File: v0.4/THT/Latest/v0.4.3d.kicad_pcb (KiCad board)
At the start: 2 copper layers, 92 x 100 mm, 116 parts, among them IC3 Trig Cond Socket, J1 Conn_01x05, J10 Conn_01x03, J3 Conn_01x02, J5 Conn_01x04, J6 Conn_01x05, J8 Conn_01x03, Q1 LFPAK88, Q3 LFPAK88, U1 SP721, U2 TC4424A, U3 SP721, U6 ULN2003, U8 LM2940S-5.0

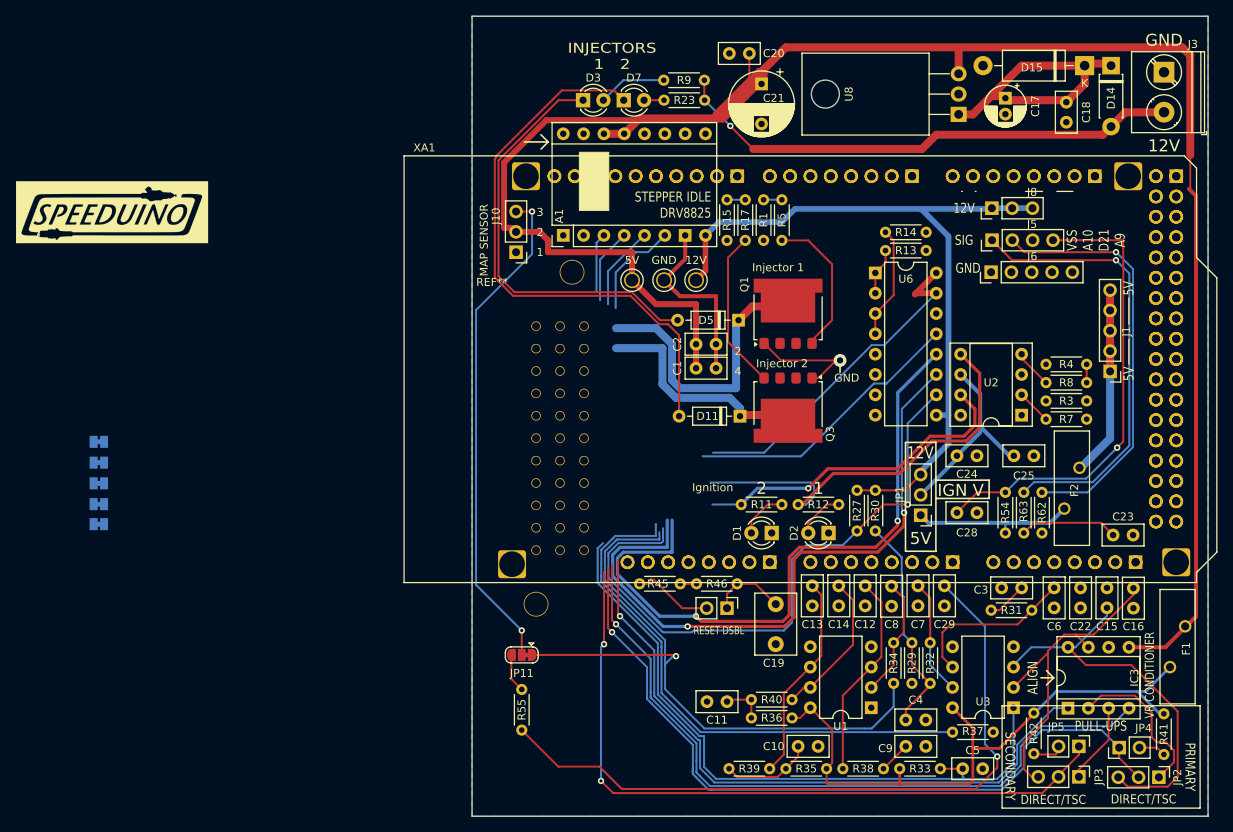
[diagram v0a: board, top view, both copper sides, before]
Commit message: split to 4v-mini
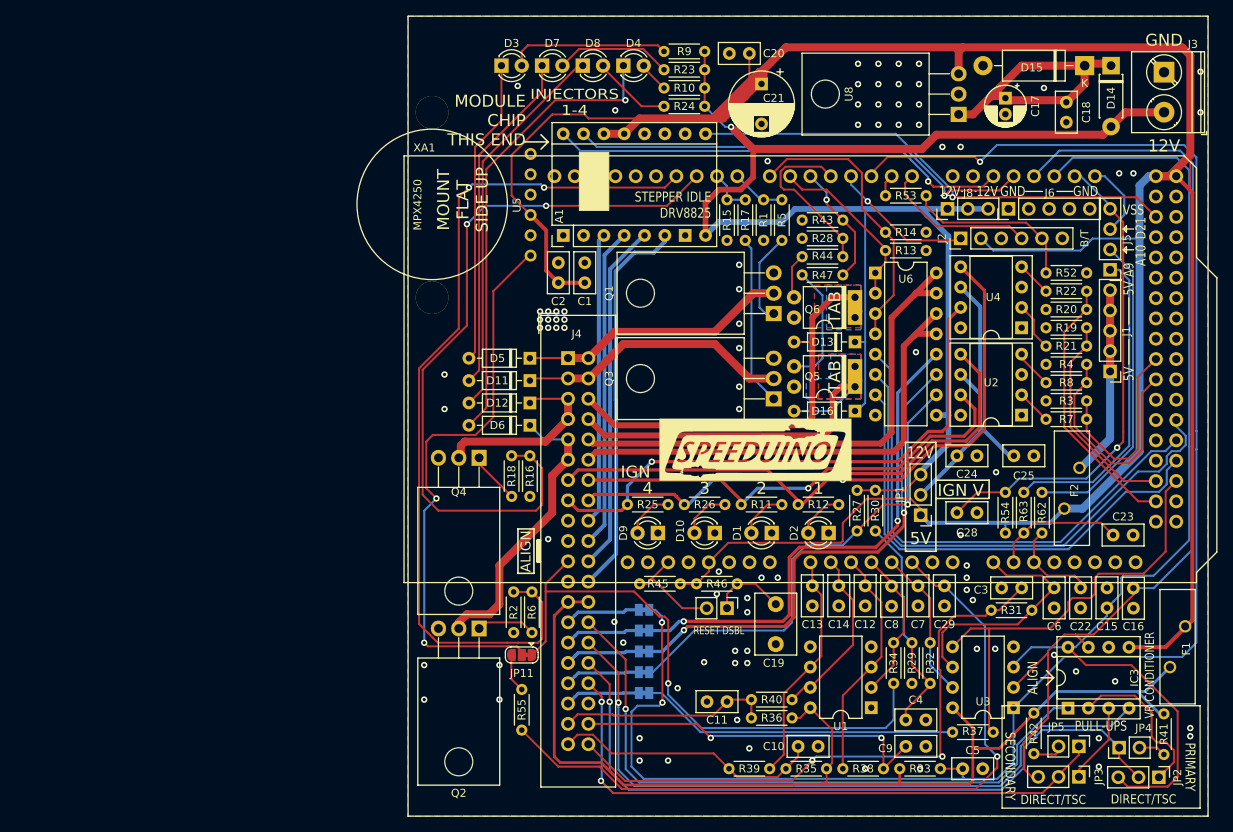
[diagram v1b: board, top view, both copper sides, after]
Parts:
- removed 12V, 5V, GND: TestPoint_Keystone_5000-5004_Miniature, TestPoint:TestPoint_Keystone_5000-5004_Miniature
- removed ? (x4): , 
- removed J10: Conn_01x03, Connector_PinHeader_2.54mm:PinHeader_1x03_P2.54mm_Vertical
- removed REF**: 6189-7106, user-made:6189-7106
- removed REF** (x5): PinHeader_1x08_P2.54mm_Vertical, Connector_PinHeader_2.54mm:PinHeader_1x08_P2.54mm_Vertical
- removed REF**: PinHeader_1x10_P2.54mm_Vertical, Connector_PinHeader_2.54mm:PinHeader_1x10_P2.54mm_Vertical
- removed REF**: PinHeader_2x18_P2.54mm_Vertical, Connector_PinHeader_2.54mm:PinHeader_2x18_P2.54mm_Vertical
- added D10: LED, LED_THT:LED_D3.0mm, F.Cu at (148.8, 101.6)
- added D12: D, Diode_THT:D_DO-35_SOD27_P7.62mm_Horizontal, F.Cu at (125.7, 85.3)
- added D13: D, Diode_THT:D_DO-35_SOD27_P7.62mm_Horizontal, F.Cu at (166.4, 77.7)
- added D16: D, Diode_THT:D_DO-35_SOD27_P7.62mm_Horizontal, F.Cu at (166.4, 86.4)
- added D4: LED, LED_THT:LED_D3.0mm, F.Cu at (137.4, 43.2)
- added D6: D, Diode_THT:D_DO-35_SOD27_P7.62mm_Horizontal, F.Cu at (125.7, 88.1)
- added D8: LED, LED_THT:LED_D3.0mm, F.Cu at (132.3, 43.2)
- added D9: LED, LED_THT:LED_D3.0mm, F.Cu at (141.7, 101.6)
- added J2: Conn_01x06, Connector_PinHeader_2.54mm:PinHeader_1x06_P2.54mm_Vertical, F.Cu at (179.6, 64.8)
- added J4: Conn_02x20_Counter_Clockwise, Connector_IDC:IDC-Header_2x20_P2.54mm_Vertical, F.Cu at (130.5, 79.7)
- added Q2: Q_NMOS_GDS, Package_TO_SOT_THT:TO-220-3_Horizontal_TabDown, F.Cu at (119.4, 113.5)
- added Q4: Q_NMOS_GDS, Package_TO_SOT_THT:TO-220-3_Horizontal_TabDown, F.Cu at (119.4, 92.2)
- added Q5: Q_NMOS_GDSD, Package_DIP:Vishay_HVM-DIP-3_W7.62mm, F.Cu at (166.4, 83.3)
- added Q6: Q_NMOS_GDSD, Package_DIP:Vishay_HVM-DIP-3_W7.62mm, F.Cu at (166.4, 74.7)
- added R10: 2.4k, Resistor_THT:R_Axial_DIN0204_L3.6mm_D1.6mm_P5.08mm_Horizontal, F.Cu at (142.5, 46.0)
- added R16: 100k, Resistor_THT:R_Axial_DIN0204_L3.6mm_D1.6mm_P5.08mm_Horizontal, F.Cu at (125.7, 97.0)
- added R18: 1k, Resistor_THT:R_Axial_DIN0204_L3.6mm_D1.6mm_P5.08mm_Horizontal, F.Cu at (123.4, 97.0)
- added R19: 100k, Resistor_THT:R_Axial_DIN0204_L3.6mm_D1.6mm_P5.08mm_Horizontal, F.Cu at (195.3, 75.9)
- added R2: 100k, Resistor_THT:R_Axial_DIN0204_L3.6mm_D1.6mm_P5.08mm_Horizontal, F.Cu at (123.7, 114.0)
- added R20: 100k, Resistor_THT:R_Axial_DIN0204_L3.6mm_D1.6mm_P5.08mm_Horizontal, F.Cu at (190.2, 73.7)
- added R21: 1k, Resistor_THT:R_Axial_DIN0204_L3.6mm_D1.6mm_P5.08mm_Horizontal, F.Cu at (190.2, 78.2)
- added R22: 1k, Resistor_THT:R_Axial_DIN0204_L3.6mm_D1.6mm_P5.08mm_Horizontal, F.Cu at (190.2, 71.4)
- added R24: 2.4k, Resistor_THT:R_Axial_DIN0204_L3.6mm_D1.6mm_P5.08mm_Horizontal, F.Cu at (142.5, 48.3)
- added R25: 2.4k, Resistor_THT:R_Axial_DIN0204_L3.6mm_D1.6mm_P5.08mm_Horizontal, F.Cu at (137.9, 98.0)
- added R26: 2.4k, Resistor_THT:R_Axial_DIN0204_L3.6mm_D1.6mm_P5.08mm_Horizontal, F.Cu at (145.0, 98.0)
- added R28: 100k, Resistor_THT:R_Axial_DIN0204_L3.6mm_D1.6mm_P5.08mm_Horizontal, F.Cu at (159.8, 64.8)
- added R43: 100k, Resistor_THT:R_Axial_DIN0204_L3.6mm_D1.6mm_P5.08mm_Horizontal, F.Cu at (159.8, 62.5)
- added R44: 1k, Resistor_THT:R_Axial_DIN0204_L3.6mm_D1.6mm_P5.08mm_Horizontal, F.Cu at (164.8, 67.1)
- added R47: 1k, Resistor_THT:R_Axial_DIN0204_L3.6mm_D1.6mm_P5.08mm_Horizontal, F.Cu at (164.8, 69.3)
- added R52: 2k, Resistor_THT:R_Axial_DIN0204_L3.6mm_D1.6mm_P5.08mm_Horizontal, F.Cu at (190.2, 69.1)
- added R53: 1k, Resistor_THT:R_Axial_DIN0204_L3.6mm_D1.6mm_P5.08mm_Horizontal, F.Cu at (170.2, 59.4)
- added R6: 1k, Resistor_THT:R_Axial_DIN0204_L3.6mm_D1.6mm_P5.08mm_Horizontal, F.Cu at (126.0, 114.0)
- added U4: TC4424A, Package_DIP:DIP-8_W7.62mm_Socket, F.Cu at (187.2, 75.9)
- added U5: MPX4250, Misc:MPX4250, F.Cu at (125.8, 66.9)
- Q1, Q3: value LFPAK88 -> Q_NMOS_GDS; footprint Package_TO_SOT_SMD:LFPAK88 -> Package_TO_SOT_THT:TO-220-3_Horizontal_TabDown
- moved G*** 85.7 mm to (153.9, 91.2)
- moved JP10 72.1 mm to (140.0, 121.6)
- moved JP7 72.1 mm to (140.0, 113.8)
- moved JP8 72.1 mm to (140.0, 116.4)
- moved JP9 72.1 mm to (140.0, 119.0)
- moved JP6 69.0 mm to (140.0, 111.2)
- moved D11 26.6 mm to (125.7, 82.5)
- moved D5 26.5 mm to (125.7, 79.8)
- moved C2 22.2 mm to (129.3, 67.8), turned to 270 degrees
- moved C1 21.1 mm to (132.6, 67.8), turned to 270 degrees
- moved J5 15.2 mm to (198.3, 68.7), turned to 180 degrees
- moved D7 11.1 mm to (127.3, 43.2)
- moved D3 11.1 mm to (122.2, 43.2)
- moved J6 8.21 mm to (185.6, 61.1)
- moved J8 5.54 mm to (177.9, 61.1)
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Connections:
- Q1 pad 1: GND -> Net-(Q1-Pad1)
- Q1 pad 2: (no net) -> INJ-1-OUT
- Q1 pad 3: (no net) -> GND
- Q3 pad 1: GND -> Net-(Q3-Pad1)
- Q3 pad 2: (no net) -> INJ-2-OUT
- Q3 pad 3: (no net) -> GND
- XA1 pad D0: (no net) -> MCU-D0
- XA1 pad D1: (no net) -> MCU-D1
- XA1 pad D3: (no net) -> MCU-D3
- XA1 pad D4: (no net) -> MCU-D4
- XA1 pad D5: (no net) -> MCU-D5
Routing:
- net ADC-Clamp-7: track 85.3 -> 215.0 mm, vias 0 -> 3
- net MCU-D11: track 0.00 -> 109.2 mm, vias 0 -> 2
- net MCU-D10: track 0.00 -> 92.4 mm, vias 0 -> 2
- net VDD: track 266.0 -> 355.9 mm
- net ADC-Clamp-9: track 49.1 -> 128.8 mm
- net ADC-Clamp-8: track 40.9 -> 120.5 mm
- net IGN-3-OUT: track 0.00 -> 75.8 mm, vias 0 -> 1
- net O2_Sensor: track 4.97 -> 75.9 mm, vias 0 -> 2
- net IGN-4-OUT: track 0.00 -> 69.2 mm, vias 0 -> 1
- net MCU-D45: track 0.00 -> 67.7 mm
- net MCU-D47: track 0.00 -> 64.4 mm
- net MCU-D24: track 0.00 -> 61.1 mm, vias 0 -> 1
- net MCU-D49: track 0.00 -> 60.7 mm
- net VDDA: track 77.6 -> 136.4 mm
- net MCU-D17: track 0.00 -> 58.6 mm, vias 0 -> 1
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- added copper zone on F.Cu, net GND
- added copper zone on B.Cu, net HC-2-OUT
- added copper zone on F.Cu, net HC-2-OUT
- added copper zone on B.Cu, net IDLE-OUT
- added copper zone on F.Cu, net IDLE-OUT
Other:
- board size 92 x 100 mm -> 100 x 100 mm
- net class Default added: clearance 0.2, trace_width 0.25, via_dia 0.8, via_drill 0.4
- board text added: "B/T"
- board text added: "IGN"
- board text added: "INJECTORS 1-4"
- board text added: "MODULE CHIP THIS END"
- board text added: "MOUNT FLAT SIDE UP"
- board text added: "TAB"
- board text removed: "1"
- board text removed: "2"
- board text removed: "3"
- board text removed: "4"
- board text removed: "INJECTORS 1 2"
- board text removed: "Ignition"
- board text removed: "Injector 1"
- board text removed: "Injector 2"
- board text removed: "MAP SENSOR"
- board text removed: "REV 0.0.1 - diarmuid kelly 2025"
- board text removed: "SIG"

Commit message: kicad work
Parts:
- removed D10, D4, D8, D9: LED, LED_THT:LED_D3.0mm
- removed D12, D13, D16, D6: D, Diode_THT:D_DO-35_SOD27_P7.62mm_Horizontal
- removed J2: Conn_01x06, Connector_PinHeader_2.54mm:PinHeader_1x06_P2.54mm_Vertical
- removed J4: Conn_02x20_Counter_Clockwise, Connector_IDC:IDC-Header_2x20_P2.54mm_Vertical
- removed Q2, Q4: Q_NMOS_GDS, Package_TO_SOT_THT:TO-220-3_Horizontal_TabDown
- removed Q5, Q6: Q_NMOS_GDSD, Package_DIP:Vishay_HVM-DIP-3_W7.62mm
- removed R10, R24, R25, R26: 2.4k, Resistor_THT:R_Axial_DIN0204_L3.6mm_D1.6mm_P5.08mm_Horizontal
- removed R16, R19, R2, R20, R28, R43: 100k, Resistor_THT:R_Axial_DIN0204_L3.6mm_D1.6mm_P5.08mm_Horizontal
- removed R18, R21, R22, R44, R47, R53, R6: 1k, Resistor_THT:R_Axial_DIN0204_L3.6mm_D1.6mm_P5.08mm_Horizontal
- removed R52: 2k, Resistor_THT:R_Axial_DIN0204_L3.6mm_D1.6mm_P5.08mm_Horizontal
- removed U4: TC4424A, Package_DIP:DIP-8_W7.62mm_Socket
- removed U5: MPX4250, Misc:MPX4250
- added 12V: TestPoint_Keystone_5000-5004_Miniature, TestPoint:TestPoint_Keystone_5000-5004_Miniature, F.Cu at (146.5, 70.0)
- added 5V: TestPoint_Keystone_5000-5004_Miniature, TestPoint:TestPoint_Keystone_5000-5004_Miniature, F.Cu at (138.5, 70.0)
- added ?: , , F.Cu at (123.5, 105.5)
- added ?: , , F.Cu at (125.0, 57.0)
- added ?: , , F.Cu at (206.5, 105.5)
- added ?: , , F.Cu at (200.0, 57.0)
- added GND: TestPoint_Keystone_5000-5004_Miniature, TestPoint:TestPoint_Keystone_5000-5004_Miniature, F.Cu at (142.5, 70.0)
- added J10: Conn_01x03, Connector_PinHeader_2.54mm:PinHeader_1x03_P2.54mm_Vertical, F.Cu at (124.0, 66.5)
- added REF**: 6189-7106, user-made:6189-7106, F.Cu at (126.5, 75.8)
- added REF**: PinHeader_1x08_P2.54mm_Vertical, Connector_PinHeader_2.54mm:PinHeader_1x08_P2.54mm_Vertical, B.Cu at (201.4, 105.2)
- added REF**: PinHeader_1x08_P2.54mm_Vertical, Connector_PinHeader_2.54mm:PinHeader_1x08_P2.54mm_Vertical, B.Cu at (173.5, 57.0)
- added REF**: PinHeader_1x08_P2.54mm_Vertical, Connector_PinHeader_2.54mm:PinHeader_1x08_P2.54mm_Vertical, B.Cu at (155.7, 105.2)
- added REF**: PinHeader_1x08_P2.54mm_Vertical, Connector_PinHeader_2.54mm:PinHeader_1x08_P2.54mm_Vertical, B.Cu at (178.6, 105.2)
- added REF**: PinHeader_1x08_P2.54mm_Vertical, Connector_PinHeader_2.54mm:PinHeader_1x08_P2.54mm_Vertical, B.Cu at (196.3, 57.0)
- added REF**: PinHeader_1x10_P2.54mm_Vertical, Connector_PinHeader_2.54mm:PinHeader_1x10_P2.54mm_Vertical, B.Cu at (151.7, 57.0)
- added REF**: PinHeader_2x18_P2.54mm_Vertical, Connector_PinHeader_2.54mm:PinHeader_2x18_P2.54mm_Vertical, B.Cu at (206.5, 57.0)
- Q1, Q3: value Q_NMOS_GDS -> LFPAK88; footprint Package_TO_SOT_THT:TO-220-3_Horizontal_TabDown -> Package_TO_SOT_SMD:LFPAK88
- moved G*** 85.7 mm to (73.5, 61.5)
- moved JP10 72.1 mm to (71.8, 98.0)
- moved JP7 72.1 mm to (71.8, 90.2)
- moved JP8 72.1 mm to (71.8, 92.8)
- moved JP9 72.1 mm to (71.8, 95.4)
- moved JP6 69.0 mm to (71.8, 100.5)
- moved D11 26.6 mm to (152.0, 87.0)
- moved D5 26.5 mm to (151.8, 75.0)
- moved C2 22.2 mm to (149.0, 78.0), turned to 180 degrees
- moved C1 21.1 mm to (149.0, 81.0), turned to 180 degrees
- moved J5 15.2 mm to (183.5, 65.0), turned to 90 degrees
- moved D7 11.1 mm to (137.5, 47.5)
- moved D3 11.1 mm to (132.4, 47.5)
- moved J6 8.21 mm to (183.4, 69.0)
- moved J8 5.54 mm to (183.5, 61.0)
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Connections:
- Q1 pad 1: Net-(Q1-Pad1) -> GND
- Q1 pad 2: INJ-1-OUT -> (no net)
- Q1 pad 3: GND -> (no net)
- Q3 pad 1: Net-(Q3-Pad1) -> GND
- Q3 pad 2: INJ-2-OUT -> (no net)
- Q3 pad 3: GND -> (no net)
- XA1 pad D0: MCU-D0 -> (no net)
- XA1 pad D1: MCU-D1 -> (no net)
- XA1 pad D3: MCU-D3 -> (no net)
- XA1 pad D4: MCU-D4 -> (no net)
- XA1 pad D5: MCU-D5 -> (no net)
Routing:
- net ADC-Clamp-7: track 215.0 -> 85.3 mm, vias 3 -> 0
- net MCU-D11: track 109.2 -> 0.00 mm, vias 2 -> 0
- net MCU-D10: track 92.4 -> 0.00 mm, vias 2 -> 0
- net VDD: track 355.9 -> 266.0 mm
- net ADC-Clamp-9: track 128.8 -> 49.1 mm
- net ADC-Clamp-8: track 120.5 -> 40.9 mm
- net IGN-3-OUT: track 75.8 -> 0.00 mm, vias 1 -> 0
- net O2_Sensor: track 75.9 -> 4.97 mm, vias 2 -> 0
- net IGN-4-OUT: track 69.2 -> 0.00 mm, vias 1 -> 0
- net MCU-D45: track 67.7 -> 0.00 mm
- net MCU-D47: track 64.4 -> 0.00 mm
- net MCU-D24: track 61.1 -> 0.00 mm, vias 1 -> 0
- net MCU-D49: track 60.7 -> 0.00 mm
- net VDDA: track 136.4 -> 77.6 mm
- net MCU-D17: track 58.6 -> 0.00 mm, vias 1 -> 0
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- removed copper zone on F.Cu, net GND
- removed copper zone on B.Cu, net HC-2-OUT
- removed copper zone on F.Cu, net HC-2-OUT
- removed copper zone on B.Cu, net IDLE-OUT
- removed copper zone on F.Cu, net IDLE-OUT
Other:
- board size 100 x 100 mm -> 92 x 100 mm
- net class Default removed
- board text added: "1"
- board text added: "2"
- board text added: "3"
- board text added: "4"
- board text added: "INJECTORS 1 2"
- board text added: "Ignition"
- board text added: "Injector 1"
- board text added: "Injector 2"
- board text added: "MAP SENSOR"
- board text added: "REV 0.0.1 - diarmuid kelly 2025"
- board text added: "SIG"
- board text removed: "B/T"
- board text removed: "IGN"
- board text removed: "INJECTORS 1-4"
- board text removed: "MODULE CHIP THIS END"
- board text removed: "MOUNT FLAT SIDE UP"
- board text removed: "TAB"
